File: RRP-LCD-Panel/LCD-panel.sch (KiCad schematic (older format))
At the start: 15 parts, among them K101 SDCARD, P101 CONN_5X2, P102 CONN_5X2, P103 LCD, Q101 2N3901, SW101 ROTARY_ENCODER, SW102 SW_PUSH, U101 1117, U102 4050

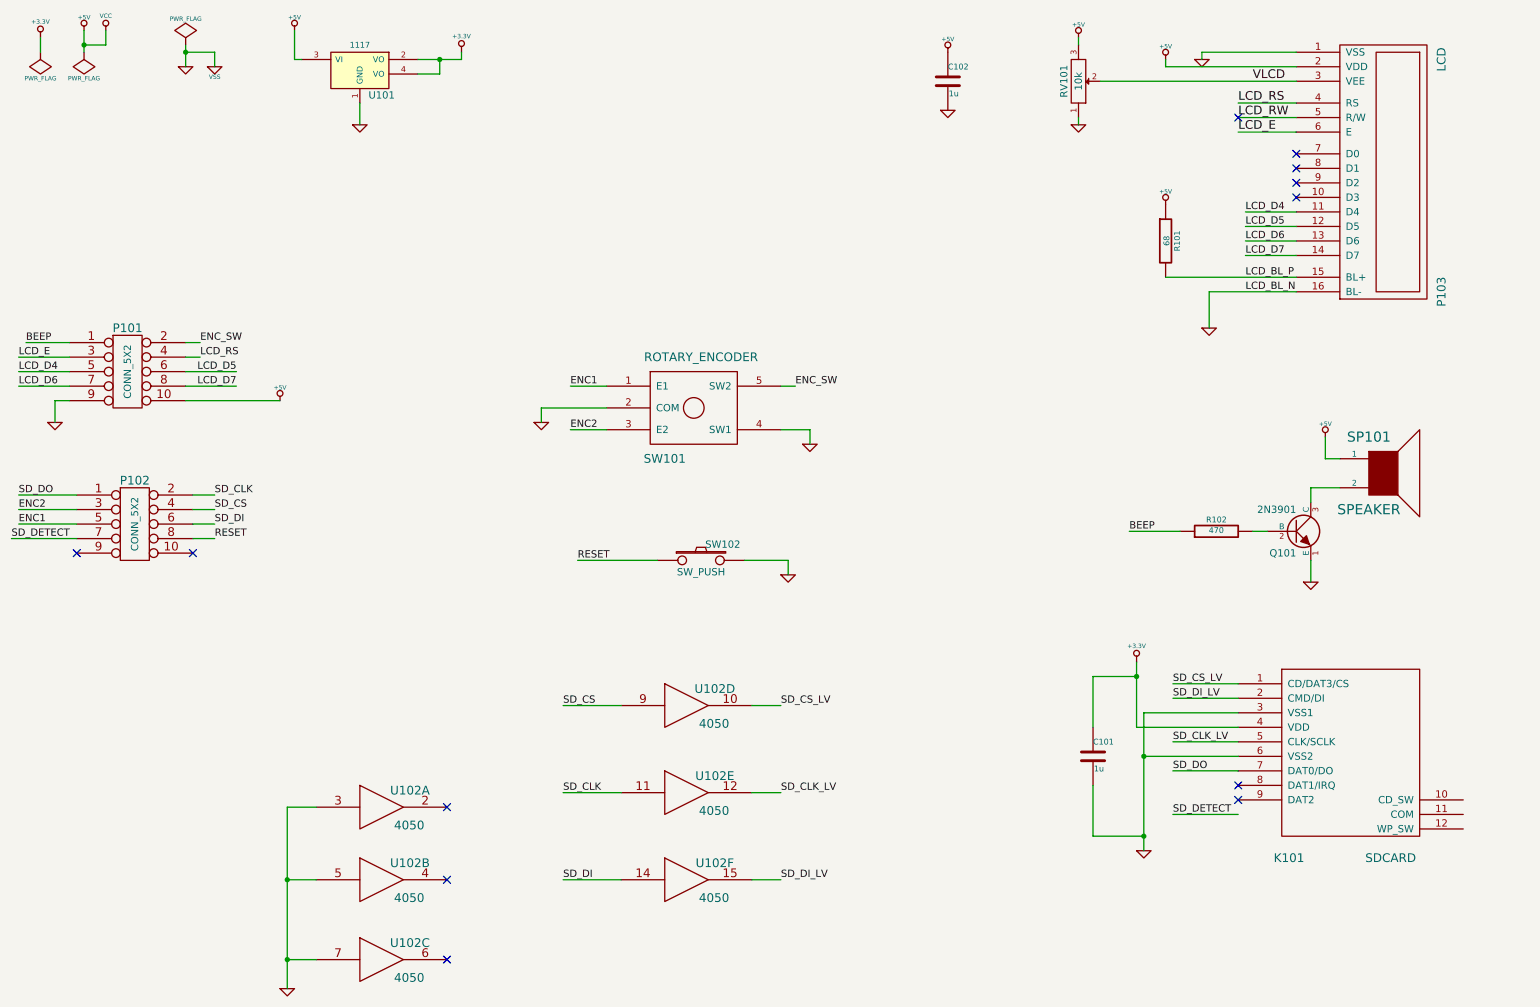
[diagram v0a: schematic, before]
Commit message: RRP-LCD-Panel: update schematics, add PDFS
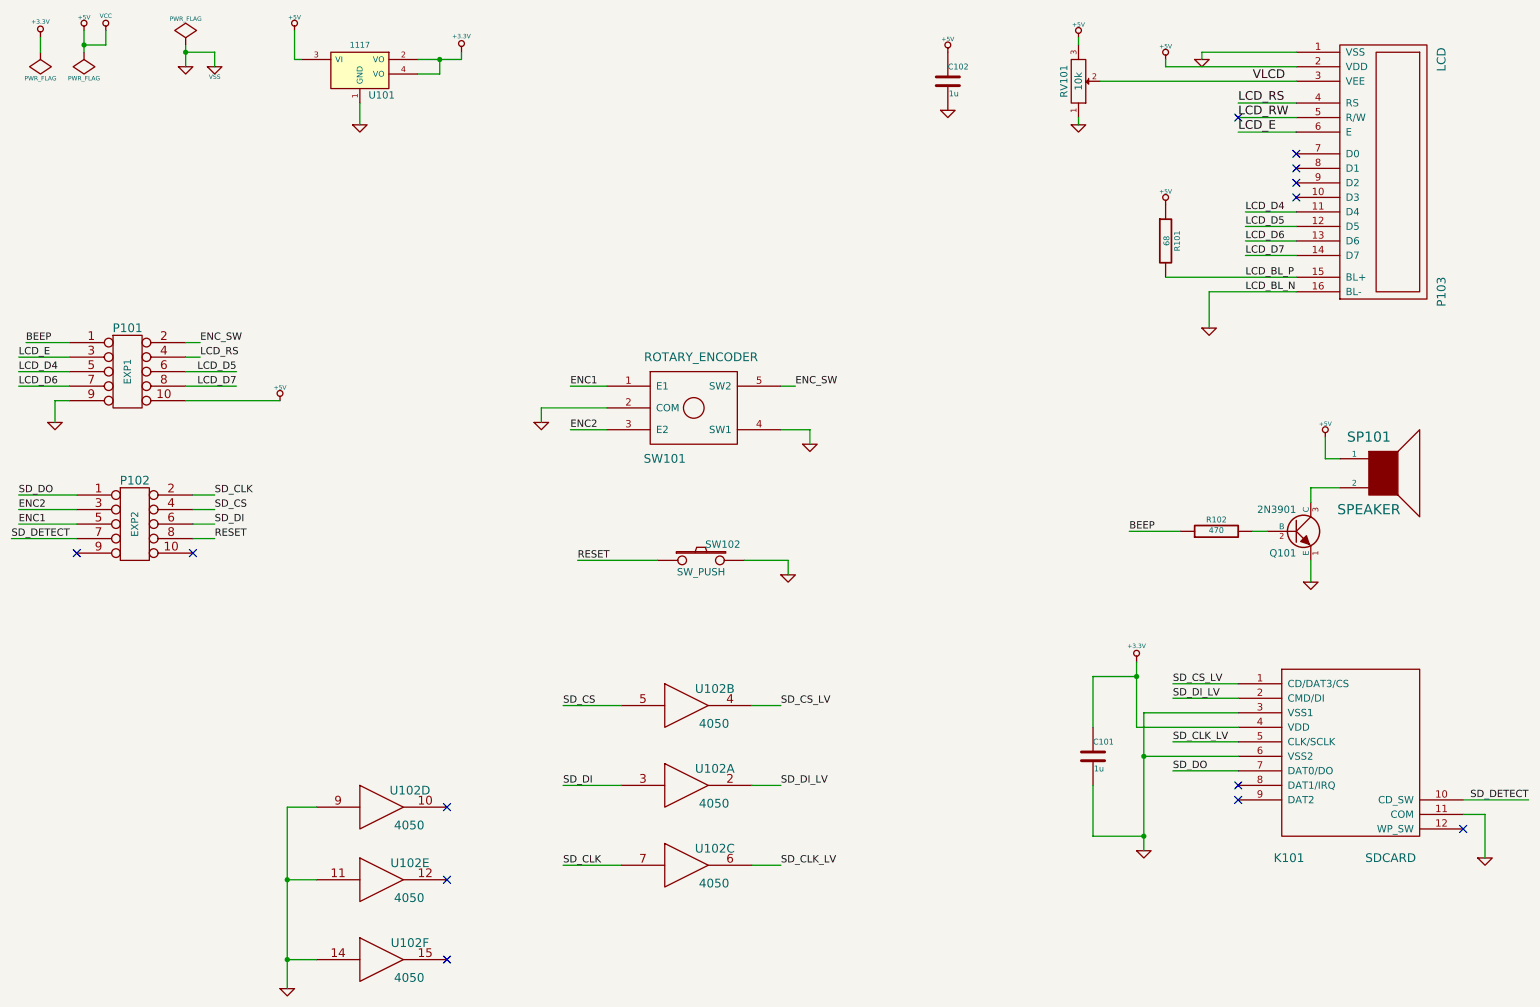
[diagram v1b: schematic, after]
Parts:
- P101: value CONN_5X2 -> EXP1
- P102: value CONN_5X2 -> EXP2
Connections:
- net GND: now also K101.11 (COM), U102.11, U102.14, U102.9; no longer U102.3, U102.5, U102.7
- net SD_CLK: now also U102.7; no longer U102.11
- net SD_CLK_LV: now also U102.6; no longer U102.12
- net SD_CS: now also U102.5; no longer U102.9
- net SD_CS_LV: now also U102.4; no longer U102.10
- net SD_DETECT: now also K101.10 (CD_SW)
- net SD_DI: now also U102.3; no longer U102.14
- net SD_DI_LV: now also U102.2; no longer U102.15
- no-connect marks 12 -> 13
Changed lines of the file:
@@
 encoding utf-8
 Sheet 1 1
-Title ""
-Date "25 sep 2013"
+Title "RepRap LCD Controller"
+Date "3 oct 2013"
 Rev ""
-Comp ""
-Comment1 ""
-Comment2 ""
+Comp "Based on http://reprap.org/wiki/RepRapDiscount_Smart_Controller"
+Comment1 "License: GPL"
+Comment2 "Drawn by: Bob Cousins"
 Comment3 ""
 Comment4 ""
@@
 P 1600 3300
 F 0 "P101" H 1600 3600 60  0000 C CNN
-F 1 "CONN_5X2" V 1600 3300 50  0000 C CNN
+F 1 "EXP1" V 1600 3300 50  0000 C CNN
 F 2 "" H 1600 3300 60  0000 C CNN
 F 3 "" H 1600 3300 60  0000 C CNN
@@
 P 1650 4350
 F 0 "P102" H 1650 4650 60  0000 C CNN
-F 1 "CONN_5X2" V 1650 4350 50  0000 C CNN
+F 1 "EXP2" V 1650 4350 50  0000 C CNN
 F 2 "" H 1650 4350 60  0000 C CNN
 F 3 "" H 1650 4350 60  0000 C CNN
@@
 Text Label 8800 6050 0    50   ~ 0
 SD_DO
-Text Label 8800 6350 0    50   ~ 0
+Text Label 11250 6250 2    50   ~ 0
 SD_DETECT
 NoConn ~ 9250 6150
@@
 	6150 4600 6150 4700
 Wire Wire Line
-	8800 6350 9250 6350
+	11250 6250 10800 6250
 Wire Wire Line
 	9250 6050 8800 6050
@@
 $Comp
 L 4050 U102
-U 4 1 52434468
+U 2 1 52434468
 P 5450 5600
 F 0 "U102" H 5645 5715 60  0000 C CNN
@@
 F 2 "" H 5450 5600 60  0000 C CNN
 F 3 "" H 5450 5600 60  0000 C CNN
-	4    5450 5600
+	2    5450 5600
 	1    0    0    -1
 $EndComp
 $Comp
 L 4050 U102
-U 5 1 52434475
-P 5450 6200
-F 0 "U102" H 5645 6315 60  0000 C CNN
-F 1 "4050" H 5640 6075 60  0000 C CNN
-F 2 "" H 5450 6200 60  0000 C CNN
-F 3 "" H 5450 6200 60  0000 C CNN
-	5    5450 6200
+U 3 1 52434475
+P 5450 6700
+F 0 "U102" H 5645 6815 60  0000 C CNN
+F 1 "4050" H 5640 6575 60  0000 C CNN
+F 2 "" H 5450 6700 60  0000 C CNN
+F 3 "" H 5450 6700 60  0000 C CNN
+	3    5450 6700
 	1    0    0    -1
 $EndComp
 $Comp
 L 4050 U102
-U 6 1 5243447B
-P 5450 6800
-F 0 "U102" H 5645 6915 60  0000 C CNN
-F 1 "4050" H 5640 6675 60  0000 C CNN
-F 2 "" H 5450 6800 60  0000 C CNN
-F 3 "" H 5450 6800 60  0000 C CNN
-	6    5450 6800
+U 1 1 5243447B
+P 5450 6150
+F 0 "U102" H 5645 6265 60  0000 C CNN
+F 1 "4050" H 5640 6025 60  0000 C CNN
+F 2 "" H 5450 6150 60  0000 C CNN
+F 3 "" H 5450 6150 60  0000 C CNN
+	1    5450 6150
 	1    0    0    -1
 $EndComp
 $Comp
 L 4050 U102
-U 1 1 52434481
+U 4 1 52434481
 P 3350 6300
 F 0 "U102" H 3545 6415 60  0000 C CNN
@@
 F 2 "" H 3350 6300 60  0000 C CNN
 F 3 "" H 3350 6300 60  0000 C CNN
-	1    3350 6300
+	4    3350 6300
 	1    0    0    -1
 $EndComp
 $Comp
 L 4050 U102
-U 2 1 52434496
+U 5 1 52434496
 P 3350 6800
 F 0 "U102" H 3545 6915 60  0000 C CNN
@@
 F 2 "" H 3350 6800 60  0000 C CNN
 F 3 "" H 3350 6800 60  0000 C CNN
-	2    3350 6800
+	5    3350 6800
 	1    0    0    -1
 $EndComp
 $Comp
 L 4050 U102
-U 3 1 524344A1
+U 6 1 524344A1
 P 3350 7350
 F 0 "U102" H 3545 7465 60  0000 C CNN
@@
 F 2 "" H 3350 7350 60  0000 C CNN
 F 3 "" H 3350 7350 60  0000 C CNN
-	3    3350 7350
+	6    3350 7350
 	1    0    0    -1
 $EndComp
@@
 Text Label 4600 5600 0    50   ~ 0
 SD_CS
-Text Label 4600 6200 0    50   ~ 0
+Text Label 4600 6700 0    50   ~ 0
 SD_CLK
-Text Label 4600 6800 0    50   ~ 0
+Text Label 4600 6150 0    50   ~ 0
 SD_DI
 Wire Wire Line
 	4600 5600 5000 5600
 Wire Wire Line
-	5000 6200 4600 6200
-Wire Wire Line
-	4600 6800 5000 6800
+	5000 6700 4600 6700
+Wire Wire Line
+	4600 6150 5000 6150
 Text Label 6100 5600 0    50   ~ 0
 SD_CS_LV
-Text Label 6100 6800 0    50   ~ 0
+Text Label 6100 6150 0    50   ~ 0
 SD_DI_LV
-Text Label 6100 6200 0    50   ~ 0
+Text Label 6100 6700 0    50   ~ 0
 SD_CLK_LV
 Wire Wire Line
 	5900 5600 6100 5600
 Wire Wire Line
-	6100 6200 5900 6200
-Wire Wire Line
-	5900 6800 6100 6800
+	6100 6700 5900 6700
+Wire Wire Line
+	5900 6150 6100 6150
 NoConn ~ 3800 6300
 NoConn ~ 3800 6800
@@
 	1450 1050 1300 1050
 Connection ~ 1300 1050
+NoConn ~ 10800 6450
+$Comp
+L GND #PWR030
+U 1 1 524DBEB6
+P 10950 6650
+F 0 "#PWR030" H 10950 6650 30  0001 C CNN
+F 1 "GND" H 10950 6580 30  0001 C CNN
+F 2 "" H 10950 6650 60  0000 C CNN
+F 3 "" H 10950 6650 60  0000 C CNN
+	1    10950 6650
+	1    0    0    -1
+$EndComp
+Wire Wire Line
+	10800 6350 10950 6350
+Wire Wire Line
+	10950 6350 10950 6650
 $EndSCHEMATC
